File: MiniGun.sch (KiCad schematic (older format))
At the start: 28 parts, among them J1 JAMMA, J2 CONN_01X06, J5 PWR_IN, J6 DC2DC, J7 SCART-F, SW1 SW_Push, SW2 SW_Push, SW3 SW_Push, U1 LD1117S33TR, U2 ESP32-WROOM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

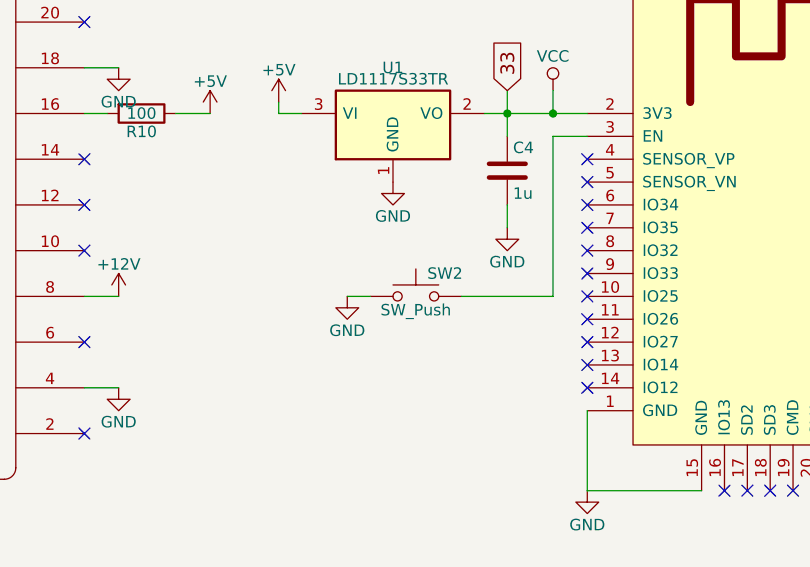
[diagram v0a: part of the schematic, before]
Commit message: Added missing reset line pullup
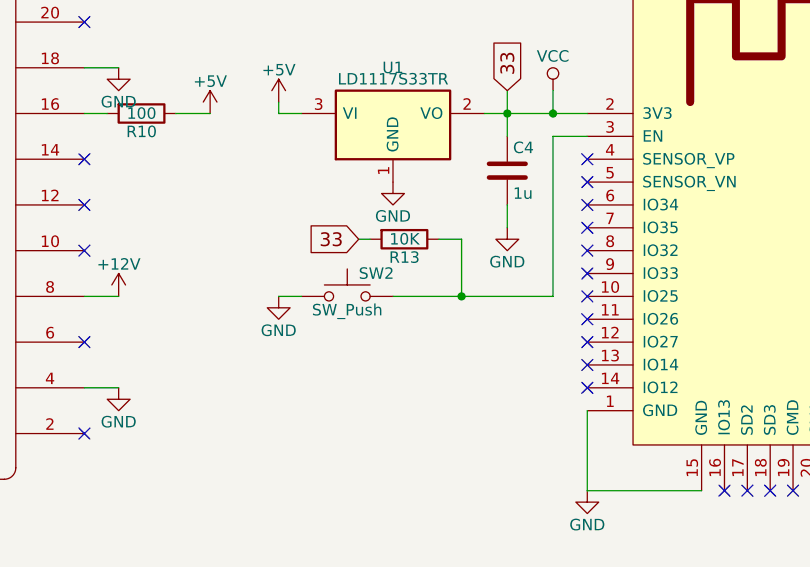
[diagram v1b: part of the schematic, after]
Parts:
- added R13: 10K, Resistors_SMD:R_1206_HandSoldering, symbol R
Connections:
- net VCC: now also R13.2
- net at SW2.2, U2.3 (EN): now also R13.1
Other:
- moved on the sheet: SW2
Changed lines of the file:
@@
 	7400 1550 7400 2250
 Wire Wire Line
-	7400 2250 7000 2250
+	7400 2250 6700 2250
 $Comp
 L SW_Push SW3
@@
 L SW_Push SW2
 U 1 1 5A520C6F
-P 6800 2250
-F 0 "SW2" H 6850 2350 50  0000 L CNN
-F 1 "SW_Push" H 6800 2190 50  0000 C CNN
-F 2 "Buttons_Switches_SMD:SW_SPST_EVQPE1" H 6800 2450 50  0001 C CNN
-F 3 "" H 6800 2450 50  0001 C CNN
-	1    6800 2250
+P 6500 2250
+F 0 "SW2" H 6550 2350 50  0000 L CNN
+F 1 "SW_Push" H 6500 2190 50  0000 C CNN
+F 2 "Buttons_Switches_SMD:SW_SPST_EVQPE1" H 6500 2450 50  0001 C CNN
+F 3 "" H 6500 2450 50  0001 C CNN
+	1    6500 2250
 	1    0    0    -1
 $EndComp
 Wire Wire Line
-	6600 2250 6500 2250
+	6300 2250 6200 2250
 $Comp
 L GND #PWR025
 U 1 1 5A520D50
-P 6500 2250
-F 0 "#PWR025" H 6500 2000 50  0001 C CNN
-F 1 "GND" H 6500 2100 50  0000 C CNN
-F 2 "" H 6500 2250 50  0001 C CNN
-F 3 "" H 6500 2250 50  0001 C CNN
-	1    6500 2250
+P 6200 2250
+F 0 "#PWR025" H 6200 2000 50  0001 C CNN
+F 1 "GND" H 6200 2100 50  0000 C CNN
+F 2 "" H 6200 2250 50  0001 C CNN
+F 3 "" H 6200 2250 50  0001 C CNN
+	1    6200 2250
 	1    0    0    -1
 $EndComp
@@
 	4150 3300 4150 3600
 NoConn ~ 9400 1900
+Text GLabel 6550 2000 0    60   Input ~ 0
+33
+$Comp
+L R R13
+U 1 1 5A85FA02
+P 6750 2000
+F 0 "R13" V 6830 2000 50  0000 C CNN
+F 1 "10K" V 6750 2000 50  0000 C CNN
+F 2 "Resistors_SMD:R_1206_HandSoldering" V 6680 2000 50  0001 C CNN
+F 3 "" H 6750 2000 50  0001 C CNN
+	1    6750 2000
+	0    1    1    0
+$EndComp
+Wire Wire Line
+	6550 2000 6600 2000
+Wire Wire Line
+	6900 2000 7000 2000
+Wire Wire Line
+	7000 2000 7000 2250
+Connection ~ 7000 2250
 $EndSCHEMATC
